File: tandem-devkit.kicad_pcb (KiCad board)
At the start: 4 copper layers, 95.4 x 100 mm, 88 parts, among them J101 Conn_01x02, J102 QWIIC I2C Connector, J301 ConnectorLCDFrontLight, J302 FPC24(0.5MM), J303 FPC10(0.5MM), Q301 2N7002, Q302 2N7002, Q303 AO3401A, U201 AMS1117-ADJ_SOT223

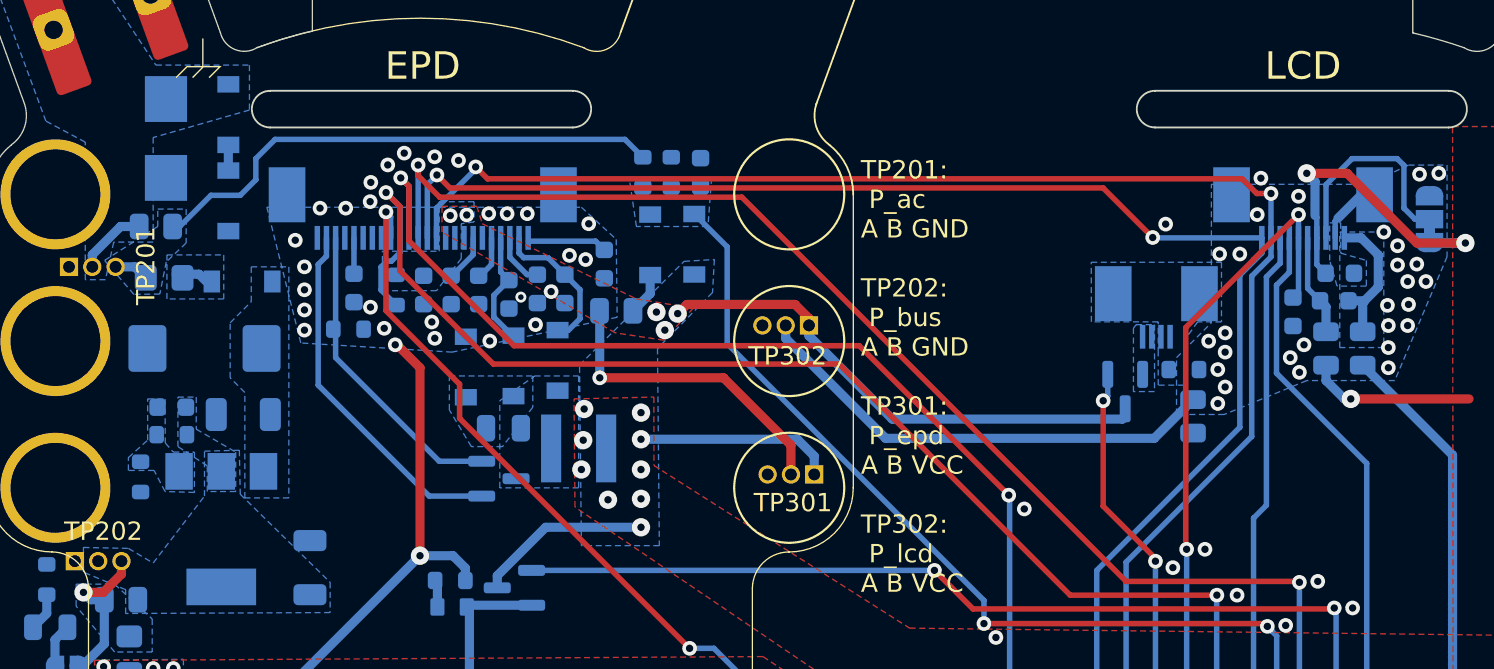
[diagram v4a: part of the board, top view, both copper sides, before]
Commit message: PCB: fix most of zone priorities and connections
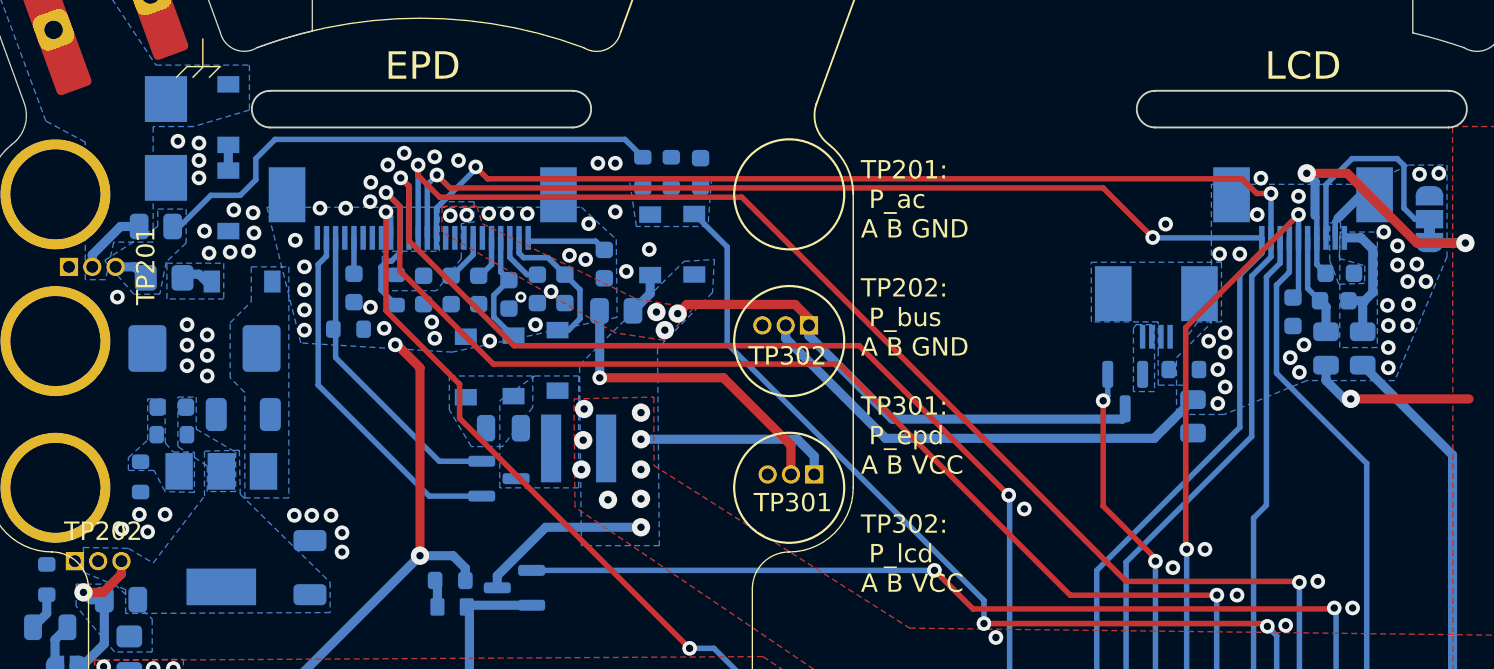
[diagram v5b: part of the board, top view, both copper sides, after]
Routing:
- net GND: vias 24 -> 56
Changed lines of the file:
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@@
   (segment (start 193.75 54.3) (end 194.1 54.3) (width 0.5) (layer "B.Cu") (net 1))
   (via (at 140.668364 42.495576) (size 0.8) (drill 0.4) (layers "F.Cu" "B.Cu") (free) (net 2))
+  (via (at 131.3 40.35) (size 0.8) (drill 0.4) (layers "F.Cu" "B.Cu") (free) (net 2))
+  (via (at 126.85 48.75) (size 0.8) (drill 0.4) (layers "F.Cu" "B.Cu") (free) (net 2))
+  (via (at 131.3 42.25) (size 0.8) (drill 0.4) (layers "F.Cu" "B.Cu") (free) (net 2))
   (via (at 142.491121 40.899532) (size 0.8) (drill 0.4) (layers "F.Cu" "B.Cu") (free) (net 2))
+  (via (at 137.45 60.65) (size 0.8) (drill 0.4) (layers "F.Cu" "B.Cu") (free) (net 2))
+  (via (at 129.45 60.6) (size 0.8) (drill 0.4) (layers "F.Cu" "B.Cu") (free) (net 2))
   (via (at 144.15 41.1) (size 0.8) (drill 0.4) (layers "F.Cu" "B.Cu") (free) (net 2))
+  (via (at 138.5 60.65) (size 0.8) (drill 0.4) (layers "F.Cu" "B.Cu") (free) (net 2))
+  (via (at 134.3 45.25) (size 0.8) (drill 0.4) (layers "F.Cu" "B.Cu") (free) (net 2))
   (via (at 192.299503 64.25) (size 0.8) (drill 0.4) (layers "F.Cu" "B.Cu") (free) (net 2))
   (via (at 178.073389 77.821555) (size 0.8) (drill 0.4) (layers "F.Cu" "B.Cu") (free) (net 2))
+  (via (at 154 44.1) (size 0.8) (drill 0.4) (layers "F.Cu" "B.Cu") (free) (net 2))
+  (via (at 154 41.45) (size 0.8) (drill 0.4) (layers "F.Cu" "B.Cu") (free) (net 2))
+  (via (at 131.75 50.81) (size 0.8) (drill 0.4) (layers "F.Cu" "B.Cu") (free) (net 2))
+  (via (at 130.65 52.49) (size 0.8) (drill 0.4) (layers "F.Cu" "B.Cu") (free) (net 2))
+  (via (at 134.25 44.15) (size 0.8) (drill 0.4) (layers "F.Cu" "B.Cu") (free) (net 2))
   (via (at 145.45 41.3) (size 0.8) (drill 0.4) (layers "F.Cu" "B.Cu") (free) (net 2))
   (via (at 194.199503 65.7) (size 0.8) (drill 0.4) (layers "F.Cu" "B.Cu") (free) (net 2))
+  (via (at 133 46.3) (size 0.8) (drill 0.4) (layers "F.Cu" "B.Cu") (free) (net 2))
+  (via (at 131.3 41.3) (size 0.8) (drill 0.4) (layers "F.Cu" "B.Cu") (free) (net 2))
+  (via (at 131.75 53.05) (size 0.8) (drill 0.4) (layers "F.Cu" "B.Cu") (free) (net 2))
+  (via (at 131.75 51.93) (size 0.8) (drill 0.4) (layers "F.Cu" "B.Cu") (free) (net 2))
+  (via (at 131.6 45.15) (size 0.8) (drill 0.4) (layers "F.Cu" "B.Cu") (free) (net 2))
   (via (at 176.551789 73.03393) (size 0.8) (drill 0.4) (layers "F.Cu" "B.Cu") (free) (net 2))
   (via (at 190.5505 66.65) (size 0.8) (drill 0.4) (layers "F.Cu" "B.Cu") (free) (net 2))
+  (via (at 154.6 47.35) (size 0.8) (drill 0.4) (layers "F.Cu" "B.Cu") (free) (net 2))
+  (via (at 130.65 51.37) (size 0.8) (drill 0.4) (layers "F.Cu" "B.Cu") (free) (net 2))
+  (via (at 130.65 50.25) (size 0.8) (drill 0.4) (layers "F.Cu" "B.Cu") (free) (net 2))
   (via (at 184.4 63.5005) (size 0.8) (drill 0.4) (layers "F.Cu" "B.Cu") (free) (net 2))
   (via (at 184.135559 78.130489) (size 0.8) (drill 0.4) (layers "F.Cu" "B.Cu") (free) (net 2))
+  (via (at 128.5 61.55) (size 0.8) (drill 0.4) (layers "F.Cu" "B.Cu") (free) (net 2))
+  (via (at 133.2 44) (size 0.8) (drill 0.4) (layers "F.Cu" "B.Cu") (free) (net 2))
+  (via (at 127.1 61.4) (size 0.8) (drill 0.4) (layers "F.Cu" "B.Cu") (free) (net 2))
+  (via (at 130.15 40.25) (size 0.8) (drill 0.4) (layers "F.Cu" "B.Cu") (free) (net 2))
+  (via (at 139.1 61.6) (size 0.8) (drill 0.4) (layers "F.Cu" "B.Cu") (free) (net 2))
+  (via (at 153.05 41.45) (size 0.8) (drill 0.4) (layers "F.Cu" "B.Cu") (free) (net 2))
   (via (at 140.631622 43.544898) (size 0.8) (drill 0.4) (layers "F.Cu" "B.Cu") (free) (net 2))
   (via (at 195.99532 71.518534) (size 0.8) (drill 0.4) (layers "F.Cu" "B.Cu") (free) (net 2))
+  (via (at 155.85 46.15) (size 0.8) (drill 0.4) (layers "F.Cu" "B.Cu") (free) (net 2))
   (via (at 187.331356 77.366593) (size 0.8) (drill 0.4) (layers "F.Cu" "B.Cu") (free) (net 2))
+  (via (at 128.05 60.6) (size 0.8) (drill 0.4) (layers "F.Cu" "B.Cu") (free) (net 2))
+  (via (at 134 46.25) (size 0.8) (drill 0.4) (layers "F.Cu" "B.Cu") (free) (net 2))
   (via (at 191.25 43.250497) (size 0.8) (drill 0.4) (layers "F.Cu" "B.Cu") (free) (net 2))
   (via (at 141.593245 41.543245) (size 0.8) (drill 0.4) (layers "F.Cu" "B.Cu") (free) (net 2))
@@
   (via (at 176.3 60.3) (size 0.8) (drill 0.4) (layers "F.Cu" "B.Cu") (free) (net 2))
   (via (at 174.7505 67.308849) (size 0.8) (drill 0.4) (layers "F.Cu" "B.Cu") (free) (net 2))
+  (via (at 136.5 60.65) (size 0.8) (drill 0.4) (layers "F.Cu" "B.Cu") (free) (net 2))
   (via (at 177.950498 72.350011) (size 0.8) (drill 0.4) (layers "F.Cu" "B.Cu") (free) (net 2))
+  (via (at 131.85 46.35) (size 0.8) (drill 0.4) (layers "F.Cu" "B.Cu") (free) (net 2))
   (via (at 198.449459 73.884925) (size 0.8) (drill 0.4) (layers "F.Cu" "B.Cu") (free) (net 2))
   (via (at 186.149503 62.5) (size 0.8) (drill 0.4) (layers "F.Cu" "B.Cu") (free) (net 2))
   (via (at 187.9 65.0005) (size 0.8) (drill 0.4) (layers "F.Cu" "B.Cu") (free) (net 2))
+  (via (at 139.1 62.65) (size 0.8) (drill 0.4) (layers "F.Cu" "B.Cu") (free) (net 2))
   (segment (start 155.9 48.5625) (end 154.9625 49.5) (width 0.5) (layer "B.Cu") (net 2))
   (segment (start 155.9 47.55) (end 155.9 48.5625) (width 0.5) (layer "B.Cu") (net 2))
@@
   (segment (start 163.4 73.175) (end 161.785 73.175) (width 0.5) (layer "B.Cu") (net 52))
   (segment (start 161.785 73.175) (end 161.755 73.145) (width 0.5) (layer "B.Cu") (net 52))
-  (segment (start 195.6 48.2) (end 195.6 46.45) (width 0.5) (layer "B.Cu") (net 53))
   (segment (start 194.75 50.6375) (end 194.75 49.05) (width 0.5) (layer "B.Cu") (net 53))
+  (segment (start 194.67 45.52) (end 193.849511 45.52) (width 0.5) (layer "B.Cu") (net 53))
   (segment (start 193.975 48.95) (end 194.85 48.95) (width 0.5) (layer "B.Cu") (net 53))
+  (segment (start 195.3 46.15) (end 194.67 45.52) (width 0.5) (layer "B.Cu") (net 53))
   (segment (start 194.75 49.05) (end 194.85 48.95) (width 0.5) (layer "B.Cu") (net 53))
-  (segment (start 194.85 48.95) (end 195.6 48.2) (width 0.5) (layer "B.Cu") (net 53))
-  (segment (start 195.6 46.45) (end 194.67 45.52) (width 0.5) (layer "B.Cu") (net 53))
-  (segment (start 194.67 45.52) (end 193.849511 45.52) (width 0.5) (layer "B.Cu") (net 53))
+  (segment (start 194.85 48.95) (end 195.3 48.5) (width 0.5) (layer "B.Cu") (net 53))
+  (segment (start 195.3 48.5) (end 195.3 46.15) (width 0.5) (layer "B.Cu") (net 53))
   (segment (start 147.35 52.4) (end 142.25048 47.30048) (width 0.3) (layer "F.Cu") (net 54))
   (segment (start 142.25048 47.30048) (end 142.25048 43.80048) (width 0.3) (layer "F.Cu") (net 54))
@@
   )
   (zone (net 1) (net_name "VCC") (layer "B.Cu") (hatch edge 0.508)
-    (priority 2)
+    (priority 3)
     (connect_pads yes (clearance 0.2))
     (min_thickness 0.2) (filled_areas_thickness no)
@@
   )
   (zone (net 68) (net_name "Net-(J301-Pad3)") (layer "B.Cu") (hatch edge 0.508)
-    (priority 1)
+    (priority 2)
     (connect_pads yes (clearance 0.2))
     (min_thickness 0.2) (filled_areas_thickness no)
@@
   )
   (zone (net 42) (net_name "/LCD_CURRENT_SENSE") (layer "B.Cu") (hatch edge 0.508)
-    (priority 1)
-    (connect_pads yes (clearance 0.2))
-    (min_thickness 0.2) (filled_areas_thickness no)
-    (fill yes (thermal_gap 0.508) (thermal_bridge_width 0.508) (smoothing fillet) (radius 0.1))
-    (polygon
-      (pts
-        (xy 193.55 46.35)
-        (xy 194.95 46.75)
-        (xy 194.95 48.15)
-        (xy 193.35 48.15)
+    (priority 3)
+    (connect_pads yes (clearance 0.2))
+    (min_thickness 0.2) (filled_areas_thickness no)
+    (fill yes (thermal_gap 0.508) (thermal_bridge_width 0.508) (smoothing fillet) (radius 0.1))
+    (polygon
+      (pts
+        (xy 193.466982 46.640567)
+        (xy 194.866982 47.040567)
+        (xy 194.85 48)
+        (xy 193.45 48.05)
         (xy 192.95 46.75)
         (xy 192.95 44.7)
@@
         (xy 132.65 48.85)
         (xy 129.55 48.85)
-        (xy 129.55 46.45)
-        (xy 132.65 46.45)
+        (xy 129.55 46.9)
+        (xy 132.65 46.9)
       )
     )
   )
   (zone (net 53) (net_name "/Display/GNDA_LCD") (layer "B.Cu") (hatch edge 0.508)
-    (priority 1)
-    (connect_pads yes (clearance 0.2))
-    (min_thickness 0.2) (filled_areas_thickness no)
-    (fill yes (thermal_gap 0.508) (thermal_bridge_width 0.508) (smoothing fillet) (radius 0.1))
-    (polygon
-      (pts
-        (xy 195.9 51.5)
+    (priority 2)
+    (connect_pads yes (clearance 0.2))
+    (min_thickness 0.2) (filled_areas_thickness no)
+    (fill yes (thermal_gap 0.508) (thermal_bridge_width 0.508) (smoothing fillet) (radius 0.1))
+    (polygon
+      (pts
+        (xy 195.55 51.5)
         (xy 193.5 51.5)
         (xy 193.5 45.2)
-        (xy 195.9 45.2)
+        (xy 195.55 45.2)
       )
     )
@@
         (xy 134.05 36.1)
         (xy 134.05 38.55)
-        (xy 128.8 40.05)
+        (xy 131 39.45)
+        (xy 128.8 39.45)
         (xy 128.8 45.75)
         (xy 126.65 45.75)

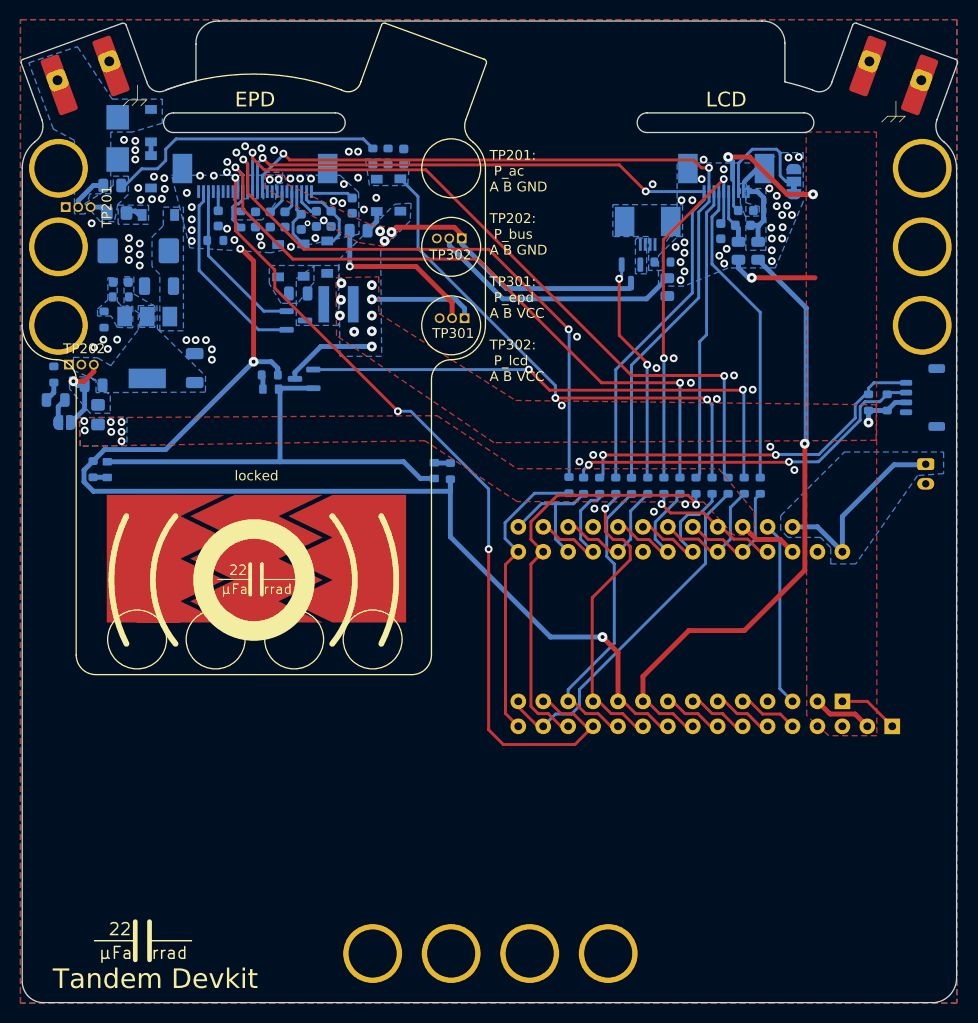
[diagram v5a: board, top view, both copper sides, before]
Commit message: PCB/footprints: Update shape and connector
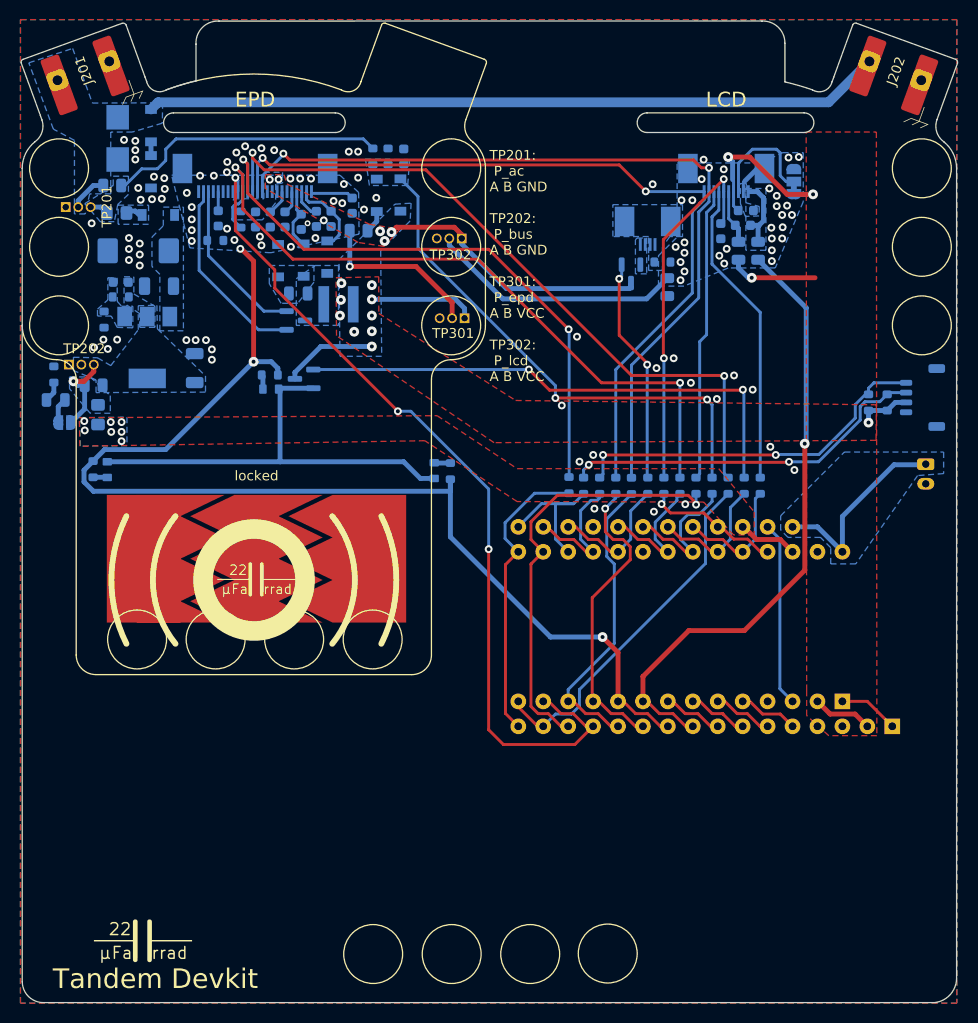
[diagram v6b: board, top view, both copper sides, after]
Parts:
- added J201: PCB Receptacle, project-lib:shimano-hub-generator-connector, F.Cu at (126.0, 33.2)
- added J202: PCB Receptacle, project-lib:shimano-hub-generator-connector, F.Cu at (208.8, 33.2)
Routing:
- net /power-A/V_DYNAMO_AC: track 3.90 -> 79.1 mm
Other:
- board size 95.4 x 100 mm -> 95.2 x 100 mm
